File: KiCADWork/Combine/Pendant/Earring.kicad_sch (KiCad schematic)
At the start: 3 parts, among them J1 Screw_Terminal_01x02, J2 Screw_Terminal_01x01

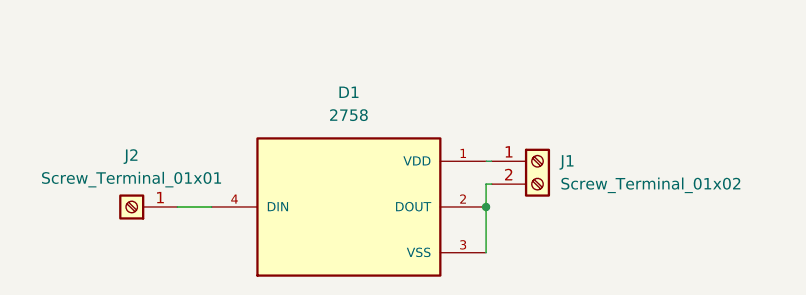
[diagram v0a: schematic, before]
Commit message: Completing the combined layout
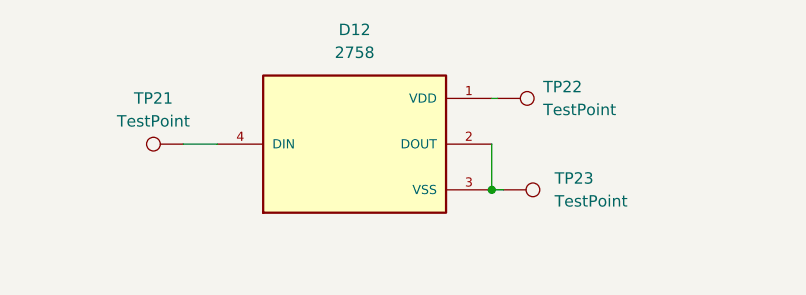
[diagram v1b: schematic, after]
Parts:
- removed D1: 2758, easyeda2kicad:SOL320P540X170-4N, symbol 2758:2758
- removed J1: Screw_Terminal_01x02, easyeda2kicad:CONN-SMD_2059-302, symbol Connector:Screw_Terminal_01x02
- removed J2: Screw_Terminal_01x01, easyeda2kicad:CONN-SMD_custom1, symbol Connector:Screw_Terminal_01x01
- added D12: 2758, easyeda2kicad:SOL320P540X170-4N, symbol 2758:2758
- added TP21, TP22, TP23: TestPoint, TestPoint:TestPoint_THTPad_D1.0mm_Drill0.5mm, symbol Connector:TestPoint
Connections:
- new net: D12.1 (VDD), TP22.1
- new net: D12.2 (DOUT), D12.3 (VSS), TP23.1
- new net: D12.4 (DIN), TP21.1

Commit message: Schem rev 1 pt1
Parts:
- added C63: 100n, Capacitor_SMD:C_0402_1005Metric_Pad0.74x0.62mm_HandSolder, symbol Device:C
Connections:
- net at D12.1 (VDD), TP22.1: now also C63.2
- net at D12.2 (DOUT), D12.3 (VSS), TP23.1: now also C63.1
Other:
- moved on the sheet: TP22, TP23
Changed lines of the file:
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@@
 (kicad_sch (version 20230121) (generator eeschema)
   (paper "A4")
+  (junction (at 184.785 79.375) (diameter 0) (color 0 0 0 0)
+  )
   (junction (at 177.165 79.375) (diameter 0) (color 0 0 0 0)
   )
+  (junction (at 184.785 69.215) (diameter 0) (color 0 0 0 0)
+  )
   (wire (pts (xy 142.875 74.295) (xy 146.685 74.295))
+    (stroke (width 0) (type default))
+  )
+  (wire (pts (xy 184.785 70.485) (xy 184.785 69.215))
+    (stroke (width 0) (type default))
+  )
+  (wire (pts (xy 184.785 79.375) (xy 177.165 79.375))
     (stroke (width 0) (type default))
   )
@@
     (stroke (width 0) (type default))
   )
-  (wire (pts (xy 177.165 69.215) (xy 177.8 69.215))
+  (wire (pts (xy 177.165 69.215) (xy 184.785 69.215))
     (stroke (width 0) (type default))
   )
-  (wire (pts (xy 178.435 79.375) (xy 177.165 79.375))
+  (wire (pts (xy 184.785 69.215) (xy 185.42 69.215))
+    (stroke (width 0) (type default))
+  )
+  (wire (pts (xy 184.785 78.105) (xy 184.785 79.375))
+    (stroke (width 0) (type default))
+  )
+  (wire (pts (xy 185.42 79.375) (xy 184.785 79.375))
     (stroke (width 0) (type default))
   )
@@
     )
   )
-  (symbol (lib_id "Connector:TestPoint") (at 177.8 69.215 270) (unit 1)
+  (symbol (lib_id "Connector:TestPoint") (at 185.42 69.215 270) (unit 1)
     (in_bom yes) (on_board yes) (dnp no) (fields_autoplaced)
-    (property "Reference" "TP22" (at 182.88 67.945 90)
+    (property "Reference" "TP22" (at 190.5 67.945 90)
       (effects (font (size 1.27 1.27)) (justify left))
     )
-    (property "Value" "TestPoint" (at 182.88 70.485 90)
+    (property "Value" "TestPoint" (at 190.5 70.485 90)
       (effects (font (size 1.27 1.27)) (justify left))
     )
-    (property "Footprint" "TestPoint:TestPoint_THTPad_D1.0mm_Drill0.5mm" (at 177.8 74.295 0)
+    (property "Footprint" "TestPoint:TestPoint_THTPad_D1.0mm_Drill0.5mm" (at 185.42 74.295 0)
       (effects (font (size 1.27 1.27)) hide)
     )
-    (property "Datasheet" "~" (at 177.8 74.295 0)
+    (property "Datasheet" "~" (at 185.42 74.295 0)
       (effects (font (size 1.27 1.27)) hide)
     )
@@
     )
   )
-  (symbol (lib_id "Connector:TestPoint") (at 178.435 79.375 270) (unit 1)
-    (in_bom yes) (on_board yes) (dnp no) (fields_autoplaced)
-    (property "Reference" "TP23" (at 184.15 78.105 90)
+  (symbol (lib_id "Device:C") (at 184.785 74.295 180) (unit 1)
+    (in_bom yes) (on_board yes) (dnp no)
+    (property "Reference" "C63" (at 181.61 75.565 0)
       (effects (font (size 1.27 1.27)) (justify left))
     )
-    (property "Value" "TestPoint" (at 184.15 80.645 90)
+    (property "Value" "100n" (at 181.61 73.025 0)
       (effects (font (size 1.27 1.27)) (justify left))
     )
-    (property "Footprint" "TestPoint:TestPoint_THTPad_D1.0mm_Drill0.5mm" (at 178.435 84.455 0)
+    (property "Footprint" "Capacitor_SMD:C_0402_1005Metric_Pad0.74x0.62mm_HandSolder" (at 183.8198 70.485 0)
       (effects (font (size 1.27 1.27)) hide)
     )
-    (property "Datasheet" "~" (at 178.435 84.455 0)
+    (property "Datasheet" "~" (at 184.785 74.295 0)
       (effects (font (size 1.27 1.27)) hide)
     )
+    (property "LCSC Part" "C5448809" (at 184.785 74.295 0)
+      (effects (font (size 1.27 1.27)) hide)
+    )
+    (pin "1")
+    (pin "2")
+    (instances
+      (project "Combine"
+        (path "/3a067f6e-27d8-46f5-91e9-67d8f6f5da54/aa3c9e51-7ed9-4461-9ac1-b5f5a82b6e73"
+          (reference "C63") (unit 1)
+        )
+        (path "/3a067f6e-27d8-46f5-91e9-67d8f6f5da54/ce302604-6b99-4a2a-b5ad-23ee0a1d5def"
+          (reference "C64") (unit 1)
+        )
+      )
+    )
+  )
+  (symbol (lib_id "Connector:TestPoint") (at 185.42 79.375 270) (unit 1)
+    (in_bom yes) (on_board yes) (dnp no) (fields_autoplaced)
+    (property "Reference" "TP23" (at 191.135 78.105 90)
+      (effects (font (size 1.27 1.27)) (justify left))
+    )
+    (property "Value" "TestPoint" (at 191.135 80.645 90)
+      (effects (font (size 1.27 1.27)) (justify left))
+    )
+    (property "Footprint" "TestPoint:TestPoint_THTPad_D1.0mm_Drill0.5mm" (at 185.42 84.455 0)
+      (effects (font (size 1.27 1.27)) hide)
+    )
+    (property "Datasheet" "~" (at 185.42 84.455 0)
+      (effects (font (size 1.27 1.27)) hide)
+    )
